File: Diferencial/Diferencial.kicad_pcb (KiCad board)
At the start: 2 copper layers, 100 x 100 mm, 72 parts, among them J1 Pedal Sensor 1, J2 Pedal Sensor 2, J3 DB9_Female, J4 DB9_Female, J5 Screw_Terminal_01x02, J6 Brake Sensor, J7 Out_Brake_Light, K1 RELAY_19.1x15.5mm, Q1 BC547, Q2 BC547, U1 LM358, U2 LM358, U3 MCP2558FD-xSN, U4 LM317_TO39, U5 UFRGS_PILL

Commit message: Diferencial Update
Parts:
- removed G***: LOGO, e-Power:ST_6.5x4.1mm_Copper
- removed G***: LOGO, e-Power:UFRGS_14.7x8.0mm_Copper
- removed G***: LOGO, e-Power:e-Power_22.8x12.0mm_Copper
- removed REF**: ESD-Logo_8.9x8mm_Copper, e-Power:ESD-Logo_8.9x8mm_Copper
- added C14: 100n, Capacitor_SMD:C_0805_2012Metric_Pad1.15x1.40mm_HandSolder, F.Cu at (252.1, 43.6)
- added C15: 1u, Capacitor_SMD:C_0805_2012Metric_Pad1.15x1.40mm_HandSolder, F.Cu at (232.4, 58.1)
- added D7: LED, e-Power:LED_0805_1.15x1.40mm_HandSolder, F.Cu at (227.6, 58.1)
- added J8: Brake Sensor 2, Connector_Phoenix_GMSTB:PhoenixContact_GMSTBA_2,5_3-G_1x03_P7.50mm_Horizontal, F.Cu at (230.0, 45.6)
- added R33: ADJ, Resistor_SMD:R_0805_2012Metric_Pad1.15x1.40mm_HandSolder, F.Cu at (252.1, 46.5)
- added R34: 2K7, Resistor_SMD:R_0805_2012Metric_Pad1.15x1.40mm_HandSolder, F.Cu at (237.1, 58.1)
- added R35: 2K2, Resistor_SMD:R_0805_2012Metric_Pad1.15x1.40mm_HandSolder, F.Cu at (241.9, 58.1)
- added R36: ADJ, Resistor_SMD:R_0805_2012Metric_Pad1.15x1.40mm_HandSolder, F.Cu at (252.1, 49.5)
- added R37: 3K3, Resistor_SMD:R_0805_2012Metric_Pad1.15x1.40mm_HandSolder, F.Cu at (246.6, 58.1)
- added R38: 10K, Resistor_SMD:R_0805_2012Metric_Pad1.15x1.40mm_HandSolder, F.Cu at (252.1, 52.4)
- added R39: 10K, Resistor_SMD:R_0805_2012Metric_Pad1.15x1.40mm_HandSolder, F.Cu at (252.1, 55.4)
- added R40: 10K, Resistor_SMD:R_0805_2012Metric_Pad1.15x1.40mm_HandSolder, F.Cu at (251.4, 58.3)
- added R41: 330, Resistor_SMD:R_0805_2012Metric_Pad1.15x1.40mm_HandSolder, F.Cu at (256.1, 58.3)
- J6: value Brake Sensor -> Brake Sensor 1
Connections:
- net /PA5 renamed Net-(R23-Pad2)
- net /PA6 renamed Net-(R22-Pad2)
- net /PA7 renamed Net-(R21-Pad2)
- C3 pad 2: /Brake_Sensor -> /Brake_Sensor_1
- C6 pad 2: /Brake_Sensor -> /Brake_Sensor_1
- R31 pad 2: /Brake_Sensor -> /Brake_Sensor_1
- R32 pad 2: Brake_Light -> /Brake_Light
- U2 pad 5: (no net) -> Net-(R33-Pad1)
- U2 pad 6: (no net) -> Net-(R38-Pad1)
- U2 pad 7: (no net) -> Net-(R38-Pad1)
- U5 pad 10: Net-(U5-Pad10) -> /Brake_Light
- U5 pad 26: /Steering_Wheel -> /Brake_Sensor_1
- U5 pad 27: /Brake_Sensor -> /Brake_Sensor_2
- U5 pad 28: Brake_Light -> Net-(R41-Pad2)

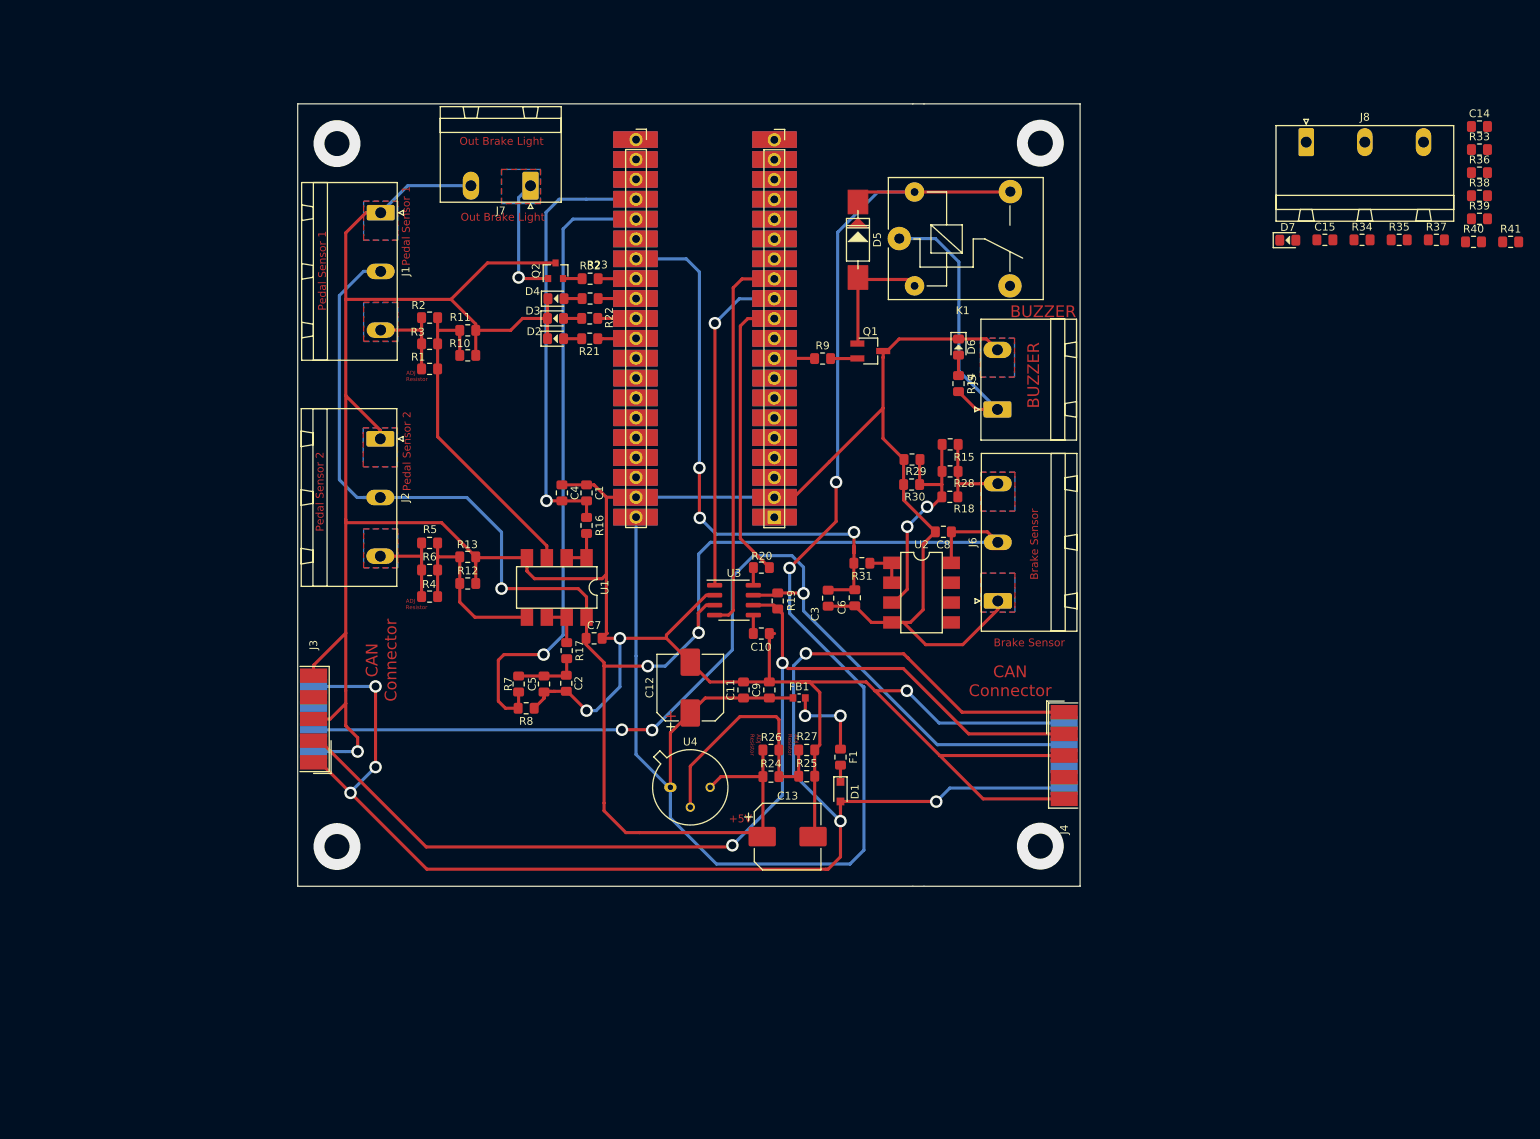
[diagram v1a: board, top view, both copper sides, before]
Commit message: Diferencial Layout Update/Main ECU Eeschema
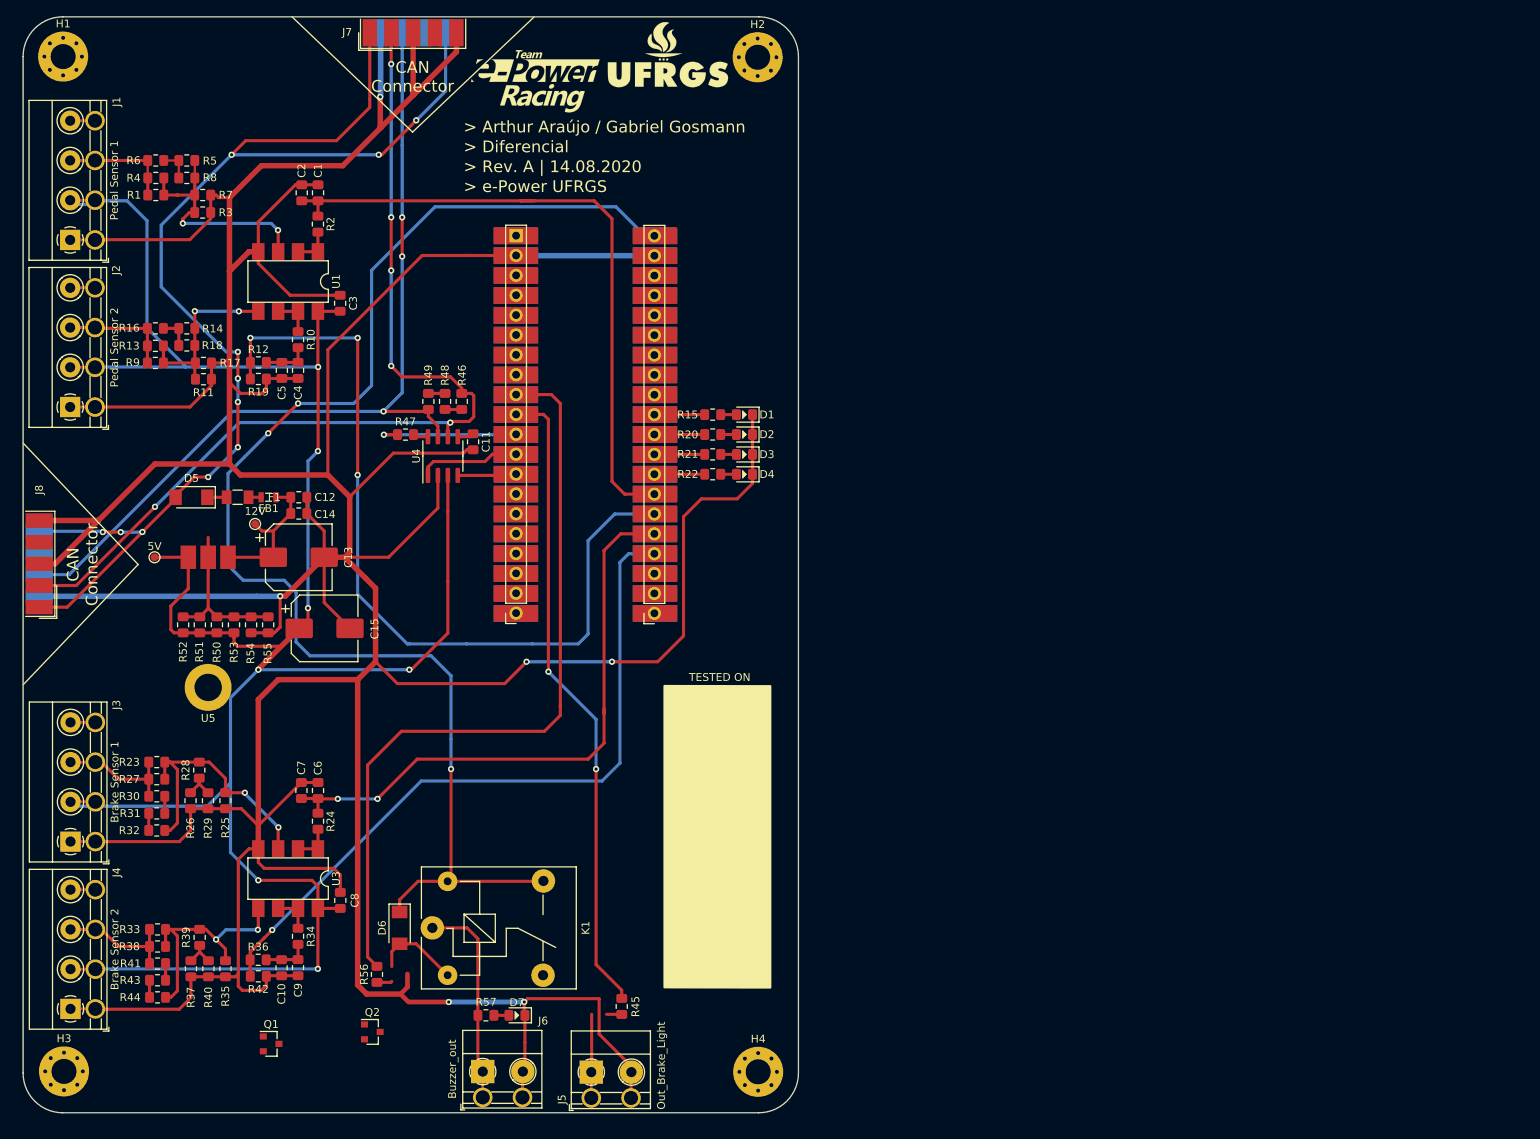
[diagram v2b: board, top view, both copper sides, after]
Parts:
- added G1: Logo_UFRGS_Large, e-Power:Logo_UFRGS_14.7x8.0mm_SilkS, F.Cu at (148.4, 34.4)
- added G2: Logo_e-Power_Large, e-Power:Logo_e-Power_16.5x8.0mm_SilkS, F.Cu at (131.4, 37.8)
- added H1: +12V, e-Power:MountingHole_3.2mm_M3_Pad_Via, F.Cu at (71.1, 34.6)
- added H2: GND, e-Power:MountingHole_3.2mm_M3_Pad_Via, F.Cu at (159.8, 34.7)
- added H3: GND, e-Power:MountingHole_3.2mm_M3_Pad_Via, F.Cu at (71.2, 164.4)
- added H4: GND, e-Power:MountingHole_3.2mm_M3_Pad_Via, F.Cu at (159.9, 164.4)
- added R42: 10K, Resistor_SMD:R_0805_2012Metric_Pad1.15x1.40mm_HandSolder, F.Cu at (96.0, 152.2)
- added R43: 1K, Resistor_SMD:R_0805_2012Metric_Pad1.15x1.40mm_HandSolder, F.Cu at (83.1, 152.7)
- added R44: 1K, Resistor_SMD:R_0805_2012Metric_Pad1.15x1.40mm_HandSolder, F.Cu at (83.1, 154.9)
- added R45: 1K, Resistor_SMD:R_0805_2012Metric_Pad1.15x1.40mm_HandSolder, F.Cu at (142.5, 156.1)
- added R46: 10R, Resistor_SMD:R_0805_2012Metric_Pad1.15x1.40mm_HandSolder, F.Cu at (122.0, 78.7)
- added R47: 1K, Resistor_SMD:R_0805_2012Metric_Pad1.15x1.40mm_HandSolder, F.Cu at (114.8, 83.0)
- added R48: 10R, Resistor_SMD:R_0805_2012Metric_Pad1.15x1.40mm_HandSolder, F.Cu at (119.9, 78.7)
- added R49: 100R, Resistor_SMD:R_0805_2012Metric_Pad1.15x1.40mm_HandSolder, F.Cu at (117.8, 78.7)
- added R50: 1K, Resistor_SMD:R_0805_2012Metric_Pad1.15x1.40mm_HandSolder, F.Cu at (90.7, 107.3)
- added R51: 1K, Resistor_SMD:R_0805_2012Metric_Pad1.15x1.40mm_HandSolder, F.Cu at (88.5, 107.3)
- added R52: 1K, Resistor_SMD:R_0805_2012Metric_Pad1.15x1.40mm_HandSolder, F.Cu at (86.4, 107.3)
- added R53: ADJ, Resistor_SMD:R_0805_2012Metric_Pad1.15x1.40mm_HandSolder, F.Cu at (92.9, 107.3)
- added R54: 1K, Resistor_SMD:R_0805_2012Metric_Pad1.15x1.40mm_HandSolder, F.Cu at (95.1, 107.3)
- added R55: ADJ, Resistor_SMD:R_0805_2012Metric_Pad1.15x1.40mm_HandSolder, F.Cu at (97.3, 107.3)
- added R56: 10K, Resistor_SMD:R_0805_2012Metric_Pad1.15x1.40mm_HandSolder, F.Cu at (111.2, 152.0)
- added R57: 1K, Resistor_SMD:R_0805_2012Metric_Pad1.15x1.40mm_HandSolder, F.Cu at (125.1, 157.2)
- added TP1: 12V, e-Power:TestPoint_Pad_D1.0mm, F.Cu at (95.6, 94.4)
- added TP2: 5V, e-Power:TestPoint_Pad_D1.0mm, F.Cu at (82.7, 98.7)
- C10, C2, C7: value 100n -> 1u
- C11: value 10n -> 100n
- C12: value 470u -> 100n; footprint Capacitor_SMD:CP_Elec_8x10 -> Capacitor_SMD:C_0805_2012Metric_Pad1.15x1.40mm_HandSolder
- C13: value 470u -> 10n; footprint Capacitor_SMD:CP_Elec_8x10 -> Capacitor_SMD:C_0805_2012Metric_Pad1.15x1.40mm_HandSolder
- C14: value 100n -> 220u; footprint Capacitor_SMD:C_0805_2012Metric_Pad1.15x1.40mm_HandSolder -> Capacitor_SMD:CP_Elec_8x10
- C15: value 1u -> 220u; footprint Capacitor_SMD:C_0805_2012Metric_Pad1.15x1.40mm_HandSolder -> Capacitor_SMD:CP_Elec_8x10
- C4, C6: value 1u -> 100n
- D1: value D_SCH_1N5819 -> LED; footprint Diode_SMD:D_SOD-323_HandSoldering -> e-Power:LED_0805_1.15x1.40mm_HandSolder
- D5: value 1N4148 -> D_SCH_SS54HF; footprint e-Power:DO-35_SMD -> e-Power:DO-214AC
- D6: value LED -> D_SCH_SS54HF; footprint e-Power:LED_0805_1.15x1.40mm_HandSolder -> e-Power:DO-214AC
- F1: footprint Fuse:Fuse_0805_2012Metric_Pad1.15x1.40mm_HandSolder -> e-Power:FUSE_1206_3216Metric
- FB1: footprint e-Power:FB_0603_1608Metric -> e-Power:FB_0805_2012Metric
- J1, J2: footprint Connector_Phoenix_GMSTB:PhoenixContact_GMSTBA_2,5_3-G_1x03_P7.50mm_Horizontal -> e-Power:TerminalBlock_Phoenix_MKDS-1,5-4-5.08_1x04_P5.08mm_Horizontal
- J3: value DB9_Female -> Brake Sensor 1; footprint e-Power:DSUB-9_Female_EdgeMount_P2.77mm -> e-Power:TerminalBlock_Phoenix_MKDS-1,5-4-5.08_1x04_P5.08mm_Horizontal
- J4: value DB9_Female -> Brake Sensor 2; footprint e-Power:DSUB-9_Female_EdgeMount_P2.77mm -> e-Power:TerminalBlock_Phoenix_MKDS-1,5-4-5.08_1x04_P5.08mm_Horizontal
- J5: value Screw_Terminal_01x02 -> Out_Brake_Light; footprint Connector_Phoenix_GMSTB:PhoenixContact_GMSTBA_2,5_2-G-7,62_1x02_P7.62mm_Horizontal -> e-Power:TerminalBlock_Phoenix_MKDS-1,5-2_1x02_P5.08mm_Horizontal
- J6: value Brake Sensor 1 -> Buzzer_out; footprint Connector_Phoenix_GMSTB:PhoenixContact_GMSTBA_2,5_3-G_1x03_P7.50mm_Horizontal -> e-Power:TerminalBlock_Phoenix_MKDS-1,5-2_1x02_P5.08mm_Horizontal
- J7: value Out_Brake_Light -> DB9_Female; footprint Connector_Phoenix_GMSTB:PhoenixContact_GMSTBA_2,5_2-G-7,62_1x02_P7.62mm_Horizontal -> e-Power:DSUB-9_Female_EdgeMount_P2.77mm
- J8: value Brake Sensor 2 -> DB9_Female; footprint Connector_Phoenix_GMSTB:PhoenixContact_GMSTBA_2,5_3-G_1x03_P7.50mm_Horizontal -> e-Power:DSUB-9_Female_EdgeMount_P2.77mm
- Q1: value BC547 -> MMBT3904; footprint Package_TO_SOT_SMD:SC-59_Handsoldering -> Package_TO_SOT_SMD:SOT-23
- Q2: value BC547 -> MMBT3904; footprint e-Power:SOT-23 -> Package_TO_SOT_SMD:SOT-23
- R10, R12, R26, R27, R29, R36, R4: value ADJ -> 10K
- R11, R35: value 2K2 -> ADJ
- R13, R28: value 2K2 -> 10K
- R14, R21, R22: value 330 -> 1K
- R15: value ADJ -> 1K
- R18: value 2K7 -> 1K
- R19: value 120 -> 10K
- R2: value 1K2 -> 10K
- R23: value 330 -> ADJ
- R24, R41: value 330 -> 10K
- R25: value 1K -> ADJ
- R3: value 18K -> ADJ
- R30, R37: value 3K3 -> 10K
- R31, R8: value 10K -> 1K
- R34: value 2K7 -> 10K
- R5: value 1K2 -> 1K
- R6: value 18K -> 10K
- R9: value 10K -> ADJ
- U2: value LM358 -> UFRGS_PILL; footprint e-Power:DIP-8_SMD -> e-Power:UFRGS_PILL
- U3: value MCP2558FD-xSN -> LM358; footprint Package_SO:SOIC-8_3.9x4.9mm_P1.27mm -> e-Power:DIP-8_SMD
- U4: value LM317_TO39 -> MCP2558FD-xSN; footprint Package_TO_SOT_THT:TO-39-3 -> Package_SO:SOIC-8_3.9x4.9mm_P1.27mm
- U5: value UFRGS_PILL -> LM317_TO39; footprint e-Power:UFRGS_PILL -> e-Power:TO-220-3_Horizontal_TabDown
- moved R33 196.2 mm to (83.1, 146.2), turned to 180 degrees
- moved R41 196.0 mm to (83.1, 150.6)
- moved R38 194.3 mm to (83.1, 148.4)
- moved R39 187.6 mm to (88.5, 147.2), turned to 270 degrees
- moved R40 186.5 mm to (89.6, 151.3), turned to 270 degrees
- moved R36 185.7 mm to (96.0, 150.1)
- moved R37 184.5 mm to (87.4, 151.3), turned to 270 degrees
- moved R35 176.6 mm to (91.8, 151.3), turned to 90 degrees
- moved J8 170.7 mm to (68.0, 99.5), turned to 270 degrees
- moved R34 162.6 mm to (101.1, 147.1), turned to 270 degrees
- moved C14 160.7 mm to (101.2, 98.7)
- moved D7 139.8 mm to (129.1, 157.2), turned to 180 degrees
- moved C15 137.2 mm to (104.5, 107.7)
- moved J4 131.1 mm to (72.0, 156.4)
- moved Q1 117.1 mm to (97.7, 160.9)
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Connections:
- C10 pad 1: Net-(C10-Pad1) -> GND
- C10 pad 2: GND -> Net-(C10-Pad2)
- C11 pad 1: +12V -> Net-(C11-Pad1)
- C13 pad 1: +5V -> +12V
- C14 pad 1: GND -> +12V
- C14 pad 2: Net-(C14-Pad2) -> GND
- C15 pad 1: GND -> +5V
- C15 pad 2: Net-(C14-Pad2) -> GND
- C2 pad 2: Net-(C2-Pad2) -> /ACC_Sensor_1
- C3 pad 1: GND -> +5V
- C3 pad 2: /Brake_Sensor_1 -> GND
- C4 pad 2: /ACC_Sensor_1 -> Net-(C4-Pad2)
- C5 pad 2: Net-(C2-Pad2) -> Net-(C4-Pad2)
- C7 pad 1: +5V -> GND
- C7 pad 2: GND -> /Brake_Sensor_1
- C9 pad 1: +12V -> GND
- C9 pad 2: GND -> Net-(C10-Pad2)
- D1 pad 1: Net-(D1-Pad1) -> GND
- D1 pad 2: /Input_Power -> Net-(D1-Pad2)
- D5 pad 1: +12V -> Net-(D5-Pad1)
- D5 pad 2: Net-(D5-Pad2) -> /Input_Power
- D6 pad 1: GND -> +12V
- F1 pad 2: Net-(D1-Pad1) -> Net-(D5-Pad1)
- J3 pad 1: /Input_Power -> GND
- J3 pad 2: /CAN_L -> +5V
- J3 pad 3: GND -> Net-(J3-Pad3)
- J3 pad 4: Net-(J3-Pad4) -> (no net)
- J4 pad 1: /Input_Power -> GND
- J4 pad 2: /CAN_L -> +5V
- J4 pad 3: GND -> Net-(J4-Pad3)
- J4 pad 4: Net-(J4-Pad4) -> (no net)
- J6 pad 1: GND -> Net-(J6-Pad1)
- J6 pad 2: +5V -> GND
- J7 pad 1: Net-(J7-Pad1) -> /Input_Power
- J7 pad 2: GND -> /CAN_L
- J8 pad 1: GND -> /Input_Power
- J8 pad 2: +5V -> /CAN_L
- J8 pad 3: Net-(J8-Pad3) -> GND
- K1 pad 1: Net-(J5-Pad1) -> Net-(J6-Pad1)
- K1 pad 2: Net-(D5-Pad2) -> Net-(D6-Pad2)
- K1 pad 3: Net-(K1-Pad3) -> (no net)
- Q1 pad 1: Net-(D5-Pad2) -> Net-(Q1-Pad1)
- Q1 pad 2: Net-(Q1-Pad2) -> GND
- Q1 pad 3: GND -> Net-(J5-Pad1)
- Q2 pad 1: Net-(J7-Pad1) -> Net-(Q2-Pad1)
- Q2 pad 2: Net-(Q2-Pad2) -> GND
- Q2 pad 3: GND -> Net-(D6-Pad2)
- R10 pad 1: GND -> Net-(R10-Pad1)
- R10 pad 2: Net-(R1-Pad1) -> Net-(C4-Pad2)
- R11 pad 1: Net-(R1-Pad1) -> GND
- R11 pad 2: GND -> Net-(R11-Pad2)
- R12 pad 1: GND -> /ACC_Sensor_2
- R12 pad 2: Net-(R12-Pad2) -> Net-(C4-Pad2)
- R13 pad 1: Net-(R12-Pad2) -> Net-(J2-Pad3)
- R13 pad 2: GND -> Net-(R11-Pad2)
- R14 pad 1: Net-(D6-Pad2) -> Net-(R14-Pad1)
- R14 pad 2: Net-(J5-Pad1) -> Net-(R11-Pad2)
- R15 pad 1: Net-(R15-Pad1) -> Net-(D1-Pad2)
- R15 pad 2: Net-(J6-Pad3) -> Net-(R15-Pad2)
- R16 pad 1: Net-(R16-Pad1) -> Net-(J2-Pad3)
- R16 pad 2: /ACC_Sensor_1 -> Net-(R14-Pad1)
- R17 pad 1: Net-(R17-Pad1) -> Net-(R11-Pad2)
- R17 pad 2: Net-(C2-Pad2) -> GND
- R18 pad 1: Net-(J6-Pad3) -> Net-(R14-Pad1)
- R18 pad 2: Net-(R15-Pad1) -> Net-(R11-Pad2)
- R19 pad 1: /CAN_L -> GND
- R19 pad 2: /CAN_H -> /ACC_Sensor_2
- R2 pad 1: Net-(J1-Pad3) -> Net-(R2-Pad1)
- R2 pad 2: Net-(R1-Pad1) -> /ACC_Sensor_1
- R20 pad 1: /S -> Net-(D2-Pad2)
- R21 pad 1: Net-(D2-Pad2) -> Net-(D3-Pad2)
- R22 pad 1: Net-(D3-Pad2) -> Net-(D4-Pad2)
- R23 pad 1: Net-(D4-Pad2) -> Net-(R23-Pad1)
- R23 pad 2: Net-(R23-Pad2) -> Net-(J3-Pad3)
- R24 pad 1: +5V -> Net-(R24-Pad1)
- R24 pad 2: Net-(R24-Pad2) -> /Brake_Sensor_1
- R25 pad 1: Net-(R24-Pad2) -> GND
- R25 pad 2: GND -> Net-(R23-Pad1)
- R26 pad 1: Net-(R24-Pad2) -> Net-(R26-Pad1)
- R26 pad 2: +5V -> GND
- R27 pad 1: GND -> Net-(J3-Pad3)
- R27 pad 2: Net-(R24-Pad2) -> Net-(R23-Pad1)
- R28 pad 1: Net-(J6-Pad3) -> Net-(R23-Pad1)
- R28 pad 2: Net-(R15-Pad1) -> Net-(R26-Pad1)
- R29 pad 1: GND -> Net-(R26-Pad1)
- R29 pad 2: Net-(R15-Pad1) -> GND
- R3 pad 1: Net-(J1-Pad3) -> GND
- R30 pad 1: Net-(R15-Pad1) -> Net-(J3-Pad3)
- R30 pad 2: GND -> Net-(R30-Pad2)
- R31 pad 1: Net-(R31-Pad1) -> Net-(R30-Pad2)
- R31 pad 2: /Brake_Sensor_1 -> Net-(R31-Pad2)
- R32 pad 1: Net-(Q2-Pad2) -> Net-(R31-Pad2)
- R32 pad 2: /Brake_Light -> Net-(R23-Pad1)
- R33 pad 2: Net-(J8-Pad3) -> Net-(J4-Pad3)
- R34 pad 1: Net-(J8-Pad3) -> Net-(R34-Pad1)
- R34 pad 2: Net-(R33-Pad1) -> Net-(C10-Pad2)
- R35 pad 1: Net-(J8-Pad3) -> GND
- R36 pad 1: GND -> /Brake_Sensor_2
- R36 pad 2: Net-(R33-Pad1) -> Net-(C10-Pad2)
- R37 pad 1: Net-(R33-Pad1) -> Net-(R37-Pad1)
- R38 pad 1: Net-(R38-Pad1) -> Net-(J4-Pad3)
- R38 pad 2: Net-(C14-Pad2) -> Net-(R33-Pad1)
- R39 pad 1: /Brake_Sensor_2 -> Net-(R33-Pad1)
- R39 pad 2: Net-(C14-Pad2) -> Net-(R37-Pad1)
- R4 pad 1: Net-(R12-Pad2) -> Net-(J1-Pad3)
- R4 pad 2: Net-(J2-Pad3) -> Net-(R1-Pad1)
- R40 pad 1: GND -> Net-(R37-Pad1)
- R40 pad 2: /Brake_Sensor_2 -> GND
- R41 pad 1: Net-(D7-Pad2) -> Net-(J4-Pad3)
- R5 pad 1: Net-(J2-Pad3) -> Net-(R5-Pad1)
- R5 pad 2: Net-(R12-Pad2) -> Net-(R1-Pad1)
- R6 pad 1: Net-(J2-Pad3) -> Net-(J1-Pad3)
- R6 pad 2: Net-(R12-Pad2) -> Net-(R5-Pad1)
- R7 pad 1: /ACC_Sensor_2 -> Net-(R1-Pad1)
- R7 pad 2: Net-(C2-Pad2) -> GND
- R8 pad 1: GND -> Net-(R5-Pad1)
- R8 pad 2: /ACC_Sensor_2 -> Net-(R1-Pad1)
- R9 pad 1: /Ready_to_Drive -> Net-(R11-Pad2)
- R9 pad 2: Net-(Q1-Pad2) -> Net-(J2-Pad3)
- U1 pad 1: Net-(R16-Pad1) -> Net-(R2-Pad1)
- U1 pad 2: Net-(R16-Pad1) -> Net-(R2-Pad1)
- U1 pad 5: Net-(R12-Pad2) -> Net-(R11-Pad2)
- U1 pad 6: Net-(R17-Pad1) -> Net-(R10-Pad1)
- U1 pad 7: Net-(R17-Pad1) -> Net-(R10-Pad1)
- U2 pad 1: Net-(R31-Pad1) -> (no net)
- U2 pad 2: Net-(R31-Pad1) -> GND
- U2 pad 3: Net-(R15-Pad1) -> (no net)
- U2 pad 4: GND -> (no net)
- U2 pad 5: Net-(R33-Pad1) -> (no net)
- U2 pad 6: Net-(R38-Pad1) -> (no net)
- U2 pad 7: Net-(R38-Pad1) -> (no net)
- U2 pad 8: +5V -> (no net)
- U3 pad 1: /TX -> Net-(R24-Pad1)
- U3 pad 2: GND -> Net-(R24-Pad1)
- U3 pad 3: +5V -> Net-(R23-Pad1)
- U3 pad 4: /RX -> GND
- U3 pad 5: Net-(C10-Pad1) -> Net-(R33-Pad1)
- U3 pad 6: /CAN_L -> Net-(R34-Pad1)
- U3 pad 7: /CAN_H -> Net-(R34-Pad1)
- U3 pad 8: Net-(R20-Pad2) -> +5V
- U4 pad 1: +12V -> /TX
- U4 pad 2: Net-(R24-Pad2) -> GND
- U5 pad 1: Net-(U5-Pad1) -> +12V
- U5 pad 2: GND -> Net-(R50-Pad2)
- U5 pad 3: Net-(U5-Pad3) -> +5V
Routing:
- net GND: track 524.6 -> 792.8 mm, vias 4 -> 6
- net /Ready_to_Drive: track 5.16 -> 99.8 mm
- net /Brake_Sensor_2: track 0.00 -> 90.9 mm, vias 0 -> 1
- net /Brake_Light: track 0.04 -> 82.3 mm, vias 0 -> 2
- net +5V: track 219.3 -> 298.0 mm, vias 3 -> 7
- net /Brake_Sensor_1: track 0.00 -> 76.0 mm, vias 0 -> 2
- net /Brake_Sensor: track 72.3 -> 0.00 mm, vias 3 -> 0
- net /RX: track 49.6 -> 7.53 mm
- net Net-(R23-Pad1): track 0.00 -> 34.3 mm, vias 0 -> 2
- net /Input_Power: track 193.9 -> 161.3 mm, vias 6 -> 11
- net Net-(R24-Pad2): track 32.6 -> 0.00 mm
- net Net-(R33-Pad1): track 0.00 -> 31.7 mm, vias 0 -> 2
- net Net-(R15-Pad1): track 29.5 -> 0.00 mm, vias 2 -> 0
- net /TX: track 42.4 -> 13.0 mm, vias 1 -> 0
- net Net-(J5-Pad1): track 35.7 -> 7.18 mm
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- removed copper zone on B.Cu, net GND
- removed copper zone on F.Cu, net GND
- removed copper zone on B.Cu, net Net-(J1-Pad3)
- removed copper zone on F.Cu, net Net-(J1-Pad3)
- removed copper zone on B.Cu, net Net-(J2-Pad3)
- removed copper zone on F.Cu, net Net-(J2-Pad3)
- removed copper zone on B.Cu, net Net-(J6-Pad3)
- removed copper zone on F.Cu, net Net-(J6-Pad3)
- removed copper zone on B.Cu, net Net-(J7-Pad1)
- removed copper zone on F.Cu, net Net-(J7-Pad1)
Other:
- board size 100 x 100 mm -> 99.1 x 140.1 mm
- board text added: "> Arthur Araújo / Gabriel Gosmann"
- board text added: "> Diferencial"
- board text added: "> Rev. A | 14.08.2020"
- board text added: "> e-Power UFRGS"
- board text added: "TESTED ON"
- board text removed: "+"
- board text removed: "+5V"
- board text removed: "ADJ Resistor"
- board text removed: "BUZZER"
- board text removed: "Brake Sensor"
- board text removed: "Out Brake Light"
- board text removed: "Pedal Sensor 1"
- board text removed: "Pedal Sensor 2"

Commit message: Diferencial Layout Update
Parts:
- added TP3: AS_1, e-Power:TestPoint_Pad_D1.0mm, F.Cu at (83.0, 99.3)
- added TP4: AS_2, e-Power:TestPoint_Pad_D1.0mm, F.Cu at (91.7, 85.1)
- added TP5: GND, e-Power:TestPoint_Pad_D1.0mm, F.Cu at (118.0, 139.0)
- added TP6: BS_1, e-Power:TestPoint_Pad_D1.0mm, F.Cu at (113.4, 136.9)
- added TP7: BS_2, e-Power:TestPoint_Pad_D1.0mm, F.Cu at (97.7, 146.2)
- added TP8: GND, e-Power:TestPoint_Pad_D1.0mm, F.Cu at (99.3, 91.5)
- added TP9: GND, e-Power:TestPoint_Pad_D1.0mm, F.Cu at (128.4, 86.3)
- J7: value DB9_Female -> Screw_Terminal_01x04; footprint e-Power:DSUB-9_Female_EdgeMount_P2.77mm -> e-Power:TerminalBlock_Phoenix_MKDS-1,5-4-5.08_1x04_P5.08mm_Horizontal
- U1, U3: footprint e-Power:DIP-8_SMD -> Package_SO:SOIC-8_3.9x4.9mm_P1.27mm
- U5: value LM317_TO39 -> LM317_3PinPackage
- moved J7 132.2 mm to (130.2, 163.0), turned to 0 degrees
- moved J8 95.6 mm to (163.1, 108.8), turned to 90 degrees
- moved Q1 95.4 mm to (150.7, 81.5)
- moved G1 93.4 mm to (70.1, 85.3), turned to 90 degrees
- moved J5 91.9 mm to (151.7, 73.6), turned to 180 degrees
- moved J6 91.8 mm to (138.3, 73.6), turned to 180 degrees
- moved G2 88.1 mm to (69.9, 100.9), turned to 90 degrees
- moved Q2 83.4 mm to (152.9, 87.5), turned to 270 degrees
- moved R56 78.5 mm to (155.9, 87.5), turned to 90 degrees
- moved R57 77.5 mm to (137.9, 80.8), turned to 0 degrees
- moved D7 76.6 mm to (133.9, 80.8), turned to 0 degrees
- moved R45 74.7 mm to (147.8, 81.6), turned to 270 degrees
- moved D5 72.0 mm to (151.1, 124.8), turned to 270 degrees
- moved U5 67.3 mm to (145.1, 140.2), turned to 270 degrees
- moved D6 65.5 mm to (153.0, 93.4), turned to 90 degrees
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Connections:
- J7 pad 1: /Input_Power -> GND
- J7 pad 3: GND -> /CAN_H
- J7 pad 4: (no net) -> /Input_Power
- U2 pad 10: /Brake_Light -> /Brake_Sensor_1
- U2 pad 24: /Brake_Sensor_2 -> /Ready_to_Drive
- U2 pad 25: /Brake_Sensor_1 -> /Brake_Light
- U2 pad 9: /Ready_to_Drive -> /Brake_Sensor_2
- U5 pad 1: +12V -> Net-(R50-Pad2)
- U5 pad 2: Net-(R50-Pad2) -> +5V
- U5 pad 3: +5V -> +12V
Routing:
- net GND: track 792.8 -> 596.0 mm, vias 6 -> 4
- net /Input_Power: track 161.3 -> 0.40 mm, vias 11 -> 0
- net /CAN_L: track 124.3 -> 9.60 mm, vias 6 -> 0
- net /CAN_H: track 111.9 -> 4.35 mm, vias 3 -> 0
- net /ACC_Sensor_2: track 106.2 -> 30.1 mm, vias 3 -> 1
- net /Brake_Sensor_2: track 90.9 -> 25.4 mm
- net /ACC_Sensor_1: track 84.0 -> 32.3 mm, vias 0 -> 1
- net /Brake_Sensor_1: track 76.0 -> 25.7 mm, vias 2 -> 0
- net /Ready_to_Drive: track 99.8 -> 63.1 mm, vias 0 -> 2
- net +12V: track 195.3 -> 159.9 mm, vias 3 -> 4
- net /RX: track 7.53 -> 37.5 mm, vias 0 -> 1
- net /S: track 18.7 -> 39.3 mm
- net /Brake_Light: track 82.3 -> 62.5 mm, vias 2 -> 3
- net /TX: track 13.0 -> 32.4 mm, vias 0 -> 1
- net Net-(R50-Pad2): track 20.8 -> 38.5 mm, vias 0 -> 2
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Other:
- board size 99.1 x 140.1 mm -> 100 x 100 mm

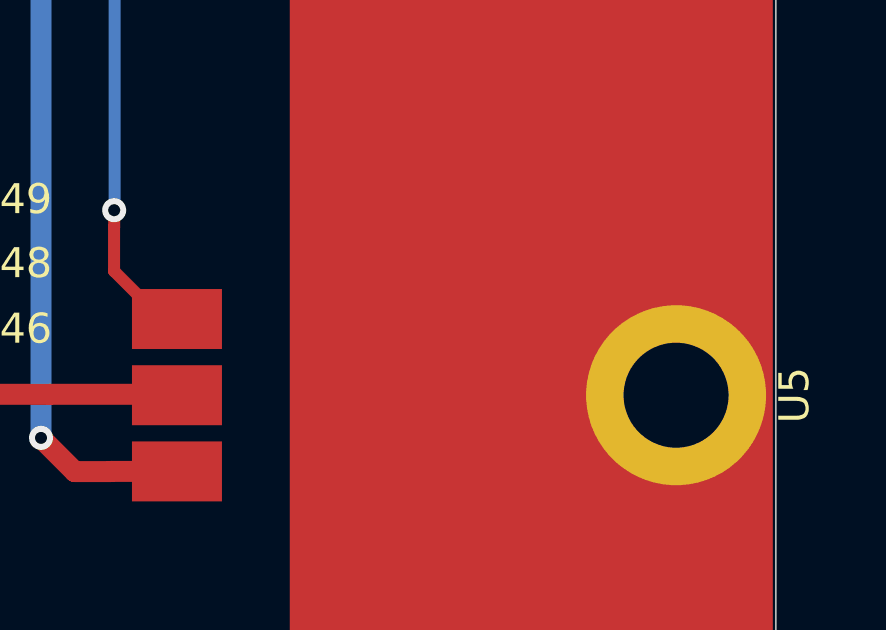
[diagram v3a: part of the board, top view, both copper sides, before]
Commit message: Layout Main ECU and Layout Luz de Freio
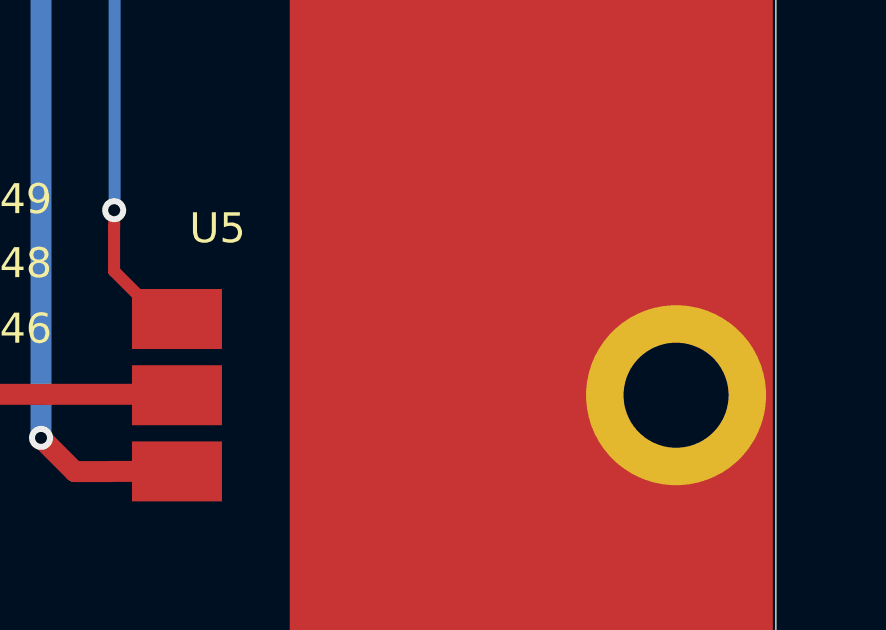
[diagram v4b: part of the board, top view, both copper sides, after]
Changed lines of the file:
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@@
   )
   (setup
-    (last_trace_width 0.4)
+    (last_trace_width 0.25)
     (user_trace_width 0.3)
     (user_trace_width 0.4)
@@
     (add_net "Net-(J5-Pad1)")
     (add_net "Net-(J6-Pad1)")
-    (add_net "Net-(J8-Pad4)")
-    (add_net "Net-(J8-Pad8)")
-    (add_net "Net-(K1-Pad3)")
     (add_net "Net-(Q1-Pad1)")
     (add_net "Net-(Q2-Pad1)")
@@
     (add_net "Net-(R5-Pad1)")
     (add_net "Net-(R50-Pad2)")
-    (add_net "Net-(U2-Pad1)")
-    (add_net "Net-(U2-Pad14)")
-    (add_net "Net-(U2-Pad15)")
-    (add_net "Net-(U2-Pad16)")
-    (add_net "Net-(U2-Pad17)")
-    (add_net "Net-(U2-Pad18)")
-    (add_net "Net-(U2-Pad19)")
-    (add_net "Net-(U2-Pad20)")
-    (add_net "Net-(U2-Pad21)")
-    (add_net "Net-(U2-Pad22)")
-    (add_net "Net-(U2-Pad23)")
-    (add_net "Net-(U2-Pad3)")
-    (add_net "Net-(U2-Pad32)")
-    (add_net "Net-(U2-Pad33)")
-    (add_net "Net-(U2-Pad34)")
-    (add_net "Net-(U2-Pad35)")
-    (add_net "Net-(U2-Pad36)")
-    (add_net "Net-(U2-Pad37)")
-    (add_net "Net-(U2-Pad38)")
-    (add_net "Net-(U2-Pad4)")
-    (add_net "Net-(U2-Pad5)")
-    (add_net "Net-(U2-Pad6)")
-    (add_net "Net-(U2-Pad7)")
-    (add_net "Net-(U2-Pad8)")
   )
   (module e-Power:TerminalBlock_Phoenix_MKDS-1,5-4-5.08_1x04_P5.08mm_Horizontal (layer F.Cu)
@@
     (descr "TO-220-3, Horizontal, RM 2.54mm, see https://www.vishay.com/docs/66542/to-220-1.pdf")
     (tags "TO-220-3 Horizontal RM 2.54mm")
-    (fp_text reference U5 (at 2.54 -20.58 90) (layer F.SilkS)
-      (effects (font (size 1 1) (thickness 0.15)))
-    )
+    (fp_text reference U5 (at -3.0226 -1.35128 180) (layer F.SilkS)
+      (effects (font (size 1 1) (thickness 0.15)))
+    )
